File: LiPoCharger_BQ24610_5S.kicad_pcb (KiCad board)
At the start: 2 copper layers, 40 x 30 mm, 58 parts, among them J1 Conn_01x04, J2 Conn_01x04, J3 Conn_01x04, Q1 SISH101DN-T1-GE3, Q2 SISH101DN-T1-GE3, Q3 SISH101DN-T1-GE3, U1 BQ24610RGER, U2 TPN2R304PL, U3 TPN2R304PL

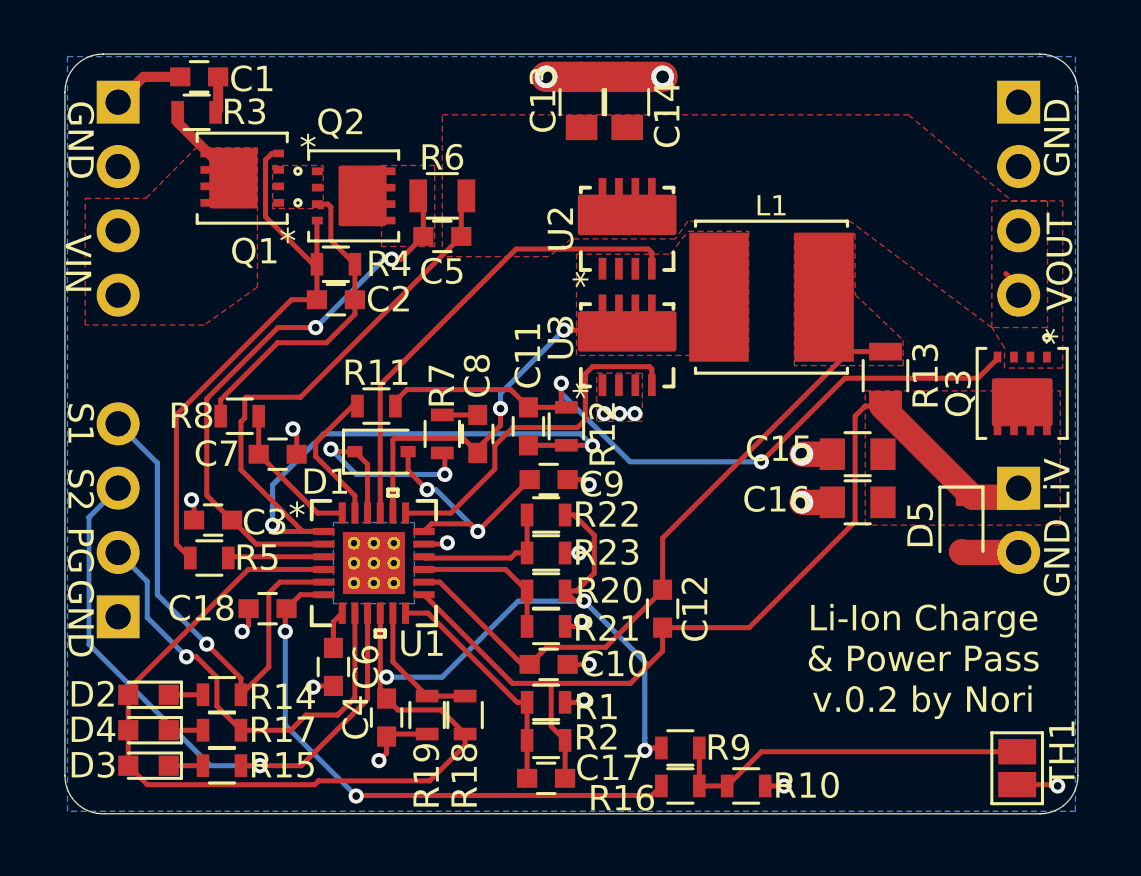
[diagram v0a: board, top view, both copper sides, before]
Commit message: Modification
Added Zener diode 27V on the power input side.
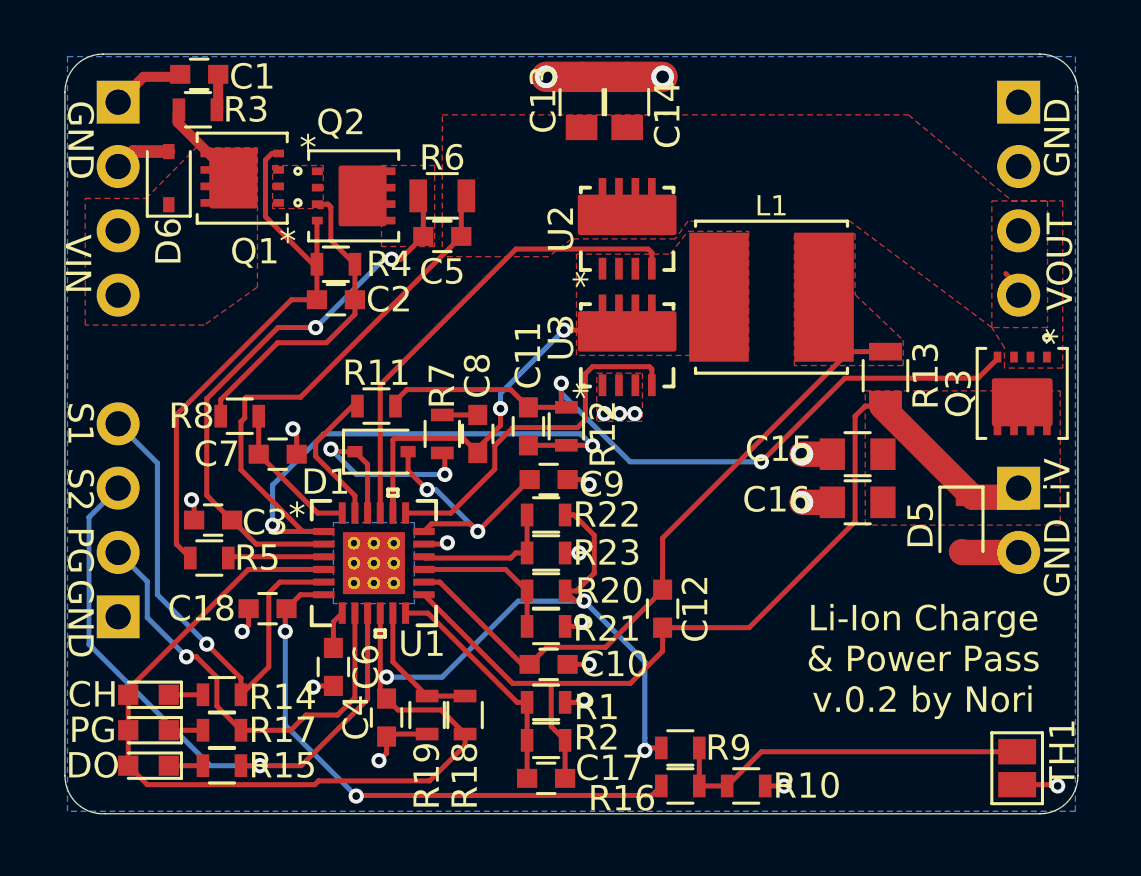
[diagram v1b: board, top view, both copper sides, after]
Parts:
- added D6: D_Zener, Diodes_SMD:D_SOD-323, F.Cu at (176.1, 83.3)
- moved R3 0.11 mm to (177.2, 80.6)
- moved C1 0.10 mm to (177.3, 79.2)
- renumbered D2 to CH, D3 to DO, D4 to PG
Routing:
- net GND: track 26.0 -> 28.3 mm
